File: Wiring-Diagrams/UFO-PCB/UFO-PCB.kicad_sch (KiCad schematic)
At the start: 10 parts, among them M1 Motor_Servo, M2 Motor_Servo, M4 Motor_Servo

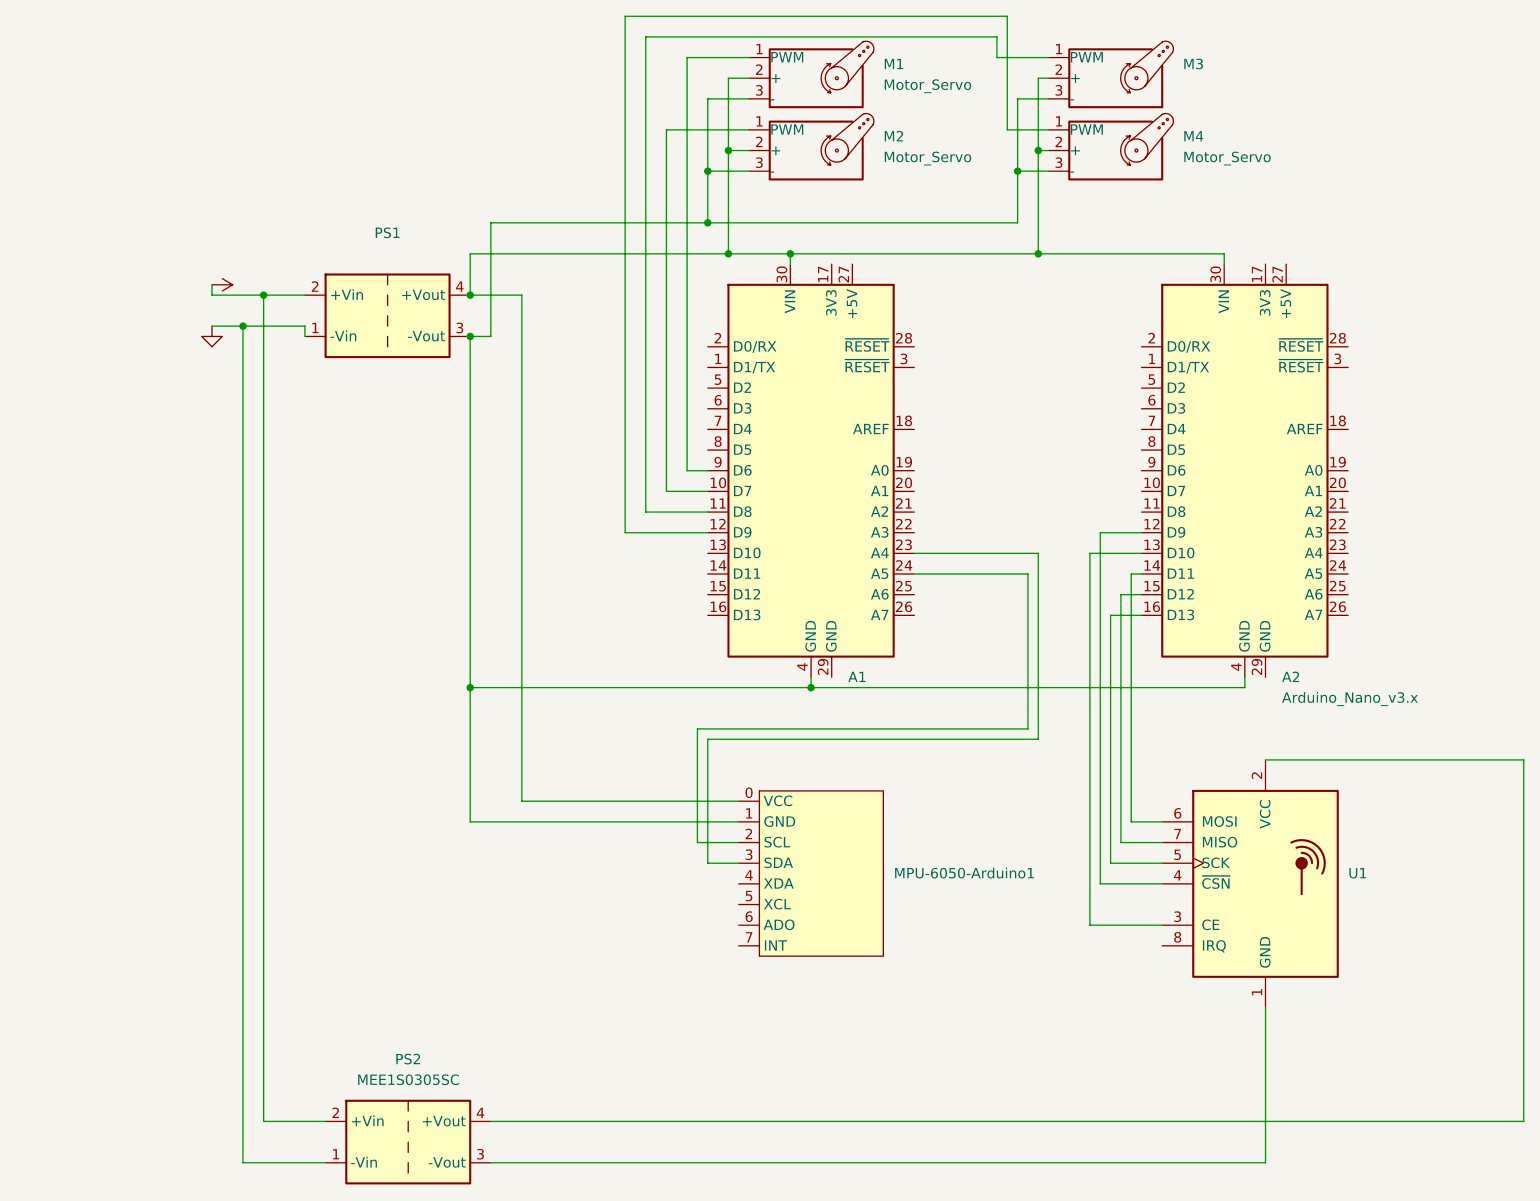
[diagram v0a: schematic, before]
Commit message: Update Controller PCB with all components, no traces yet
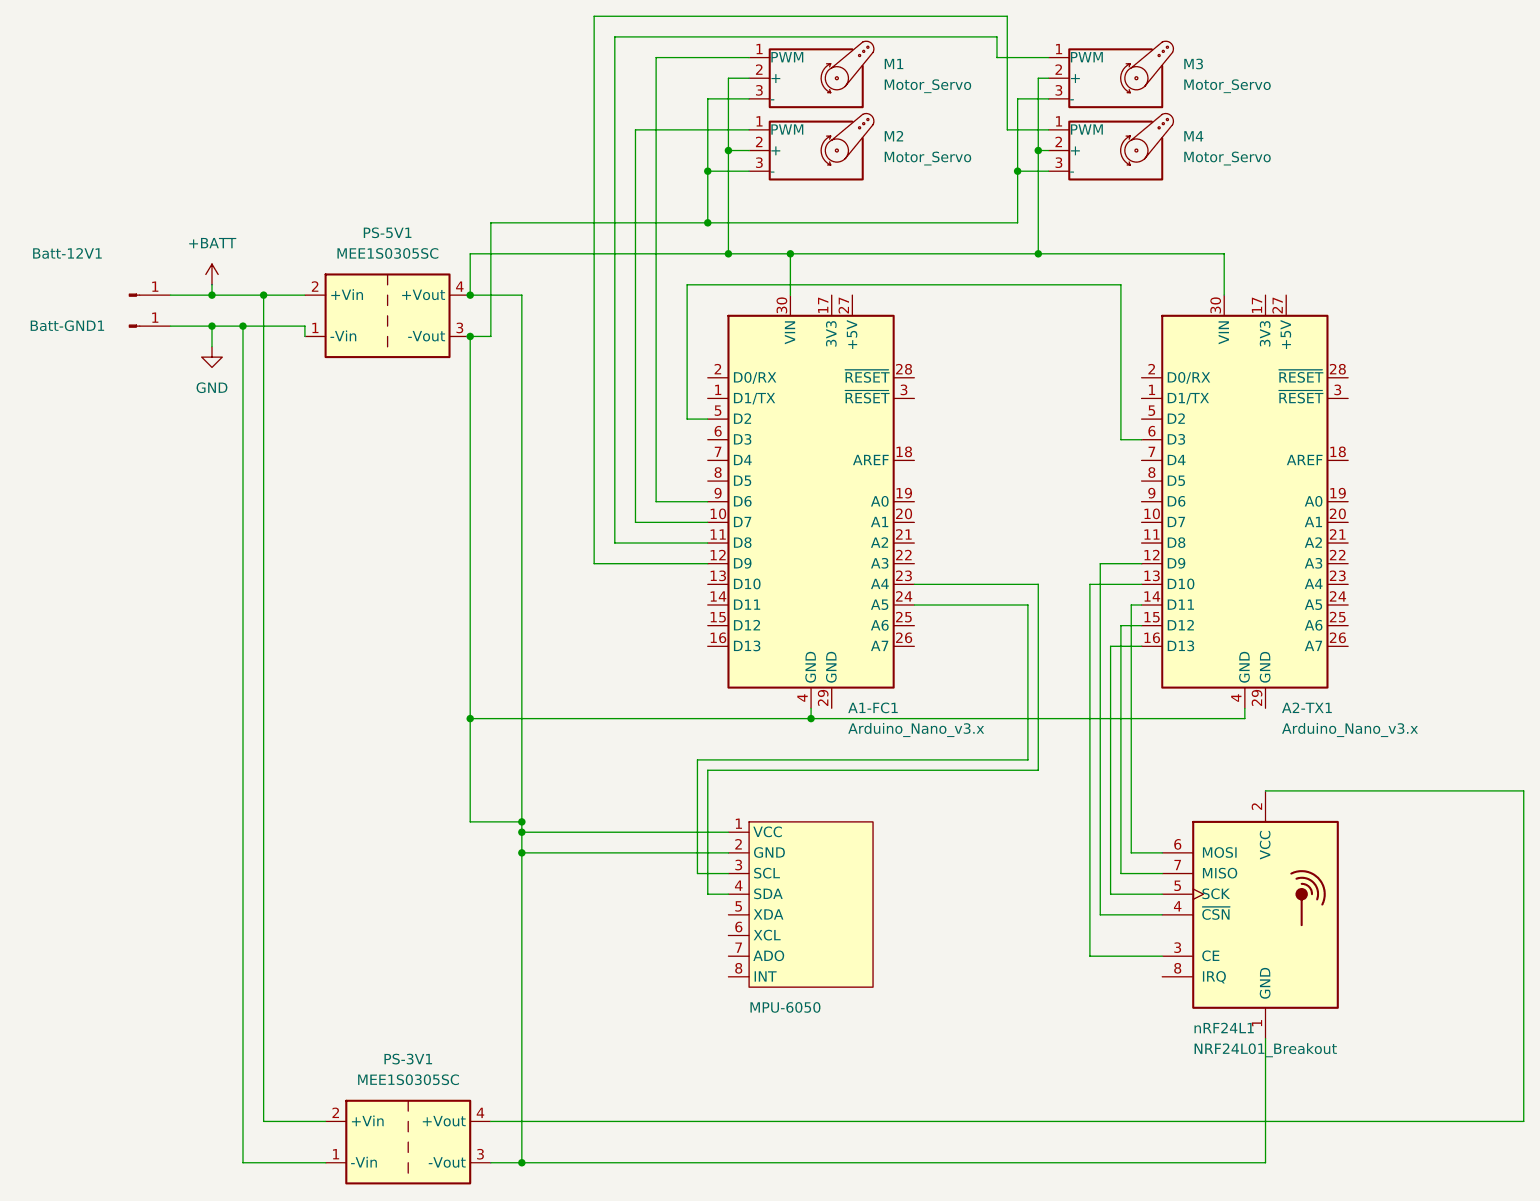
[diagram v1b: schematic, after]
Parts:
- removed MPU-6050-Arduino1: (no value), symbol Sensor_Motion:MPU-6050-Arduino
- added Batt-12V1, Batt-GND1: (no value), symbol Connector:Conn_01x01_Male
- added MPU-6050: (no value), symbol Sensor_Motion:MPU-6050-Breakout
- A1-FC1: renamed from A1; value (none) -> Arduino_Nano_v3.x; footprint (none) -> Module:Arduino_Nano
- M3: value (none) -> Motor_Servo; footprint (none) -> Connector_PinHeader_2.54mm:PinHeader_1x03_P2.54mm_Vertical
- PS-5V1: renamed from PS1; value (none) -> MEE1S0305SC; footprint (none) -> Converter_DCDC:Converter_DCDC_Murata_MEE1SxxxxSC_THT
- nRF24L1: renamed from U1; value (none) -> NRF24L01_Breakout; footprint (none) -> RF_Module:nRF24L01_Breakout
- renumbered A2 to A2-TX1, PS2 to PS-3V1
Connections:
- net +BATT: now also Batt-12V1.1 (Pin_1)
- net GND: now also Batt-GND1.1 (Pin_1)
- net at A1-FC1.30 (VIN), A2-TX1.30 (VIN), M1.2 (+)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: now also A1-FC1.4 (GND), A2-TX1.4 (GND), M1.3 (-), M2.3 (-), M3.3 (-), M4.3 (-), PS-3V1.3 (-Vout), PS-5V1.3 (-Vout), nRF24L1.1 (GND), MPU-6050.1 (VCC), MPU-6050.2 (GND)
- net at A1-FC1.23 (A4): now also MPU-6050.4 (SDA)
- net at A1-FC1.24 (A5): now also MPU-6050.3 (SCL)
- net at A1-FC1.5 (D2): now also A2-TX1.6 (D3)
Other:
- moved on the sheet: A1-FC1, A2-TX1, nRF24L1
